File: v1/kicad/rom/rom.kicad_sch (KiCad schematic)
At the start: 2 parts, among them IC1 AT28C64B-15PU, U1 LNCPU Type A Connector

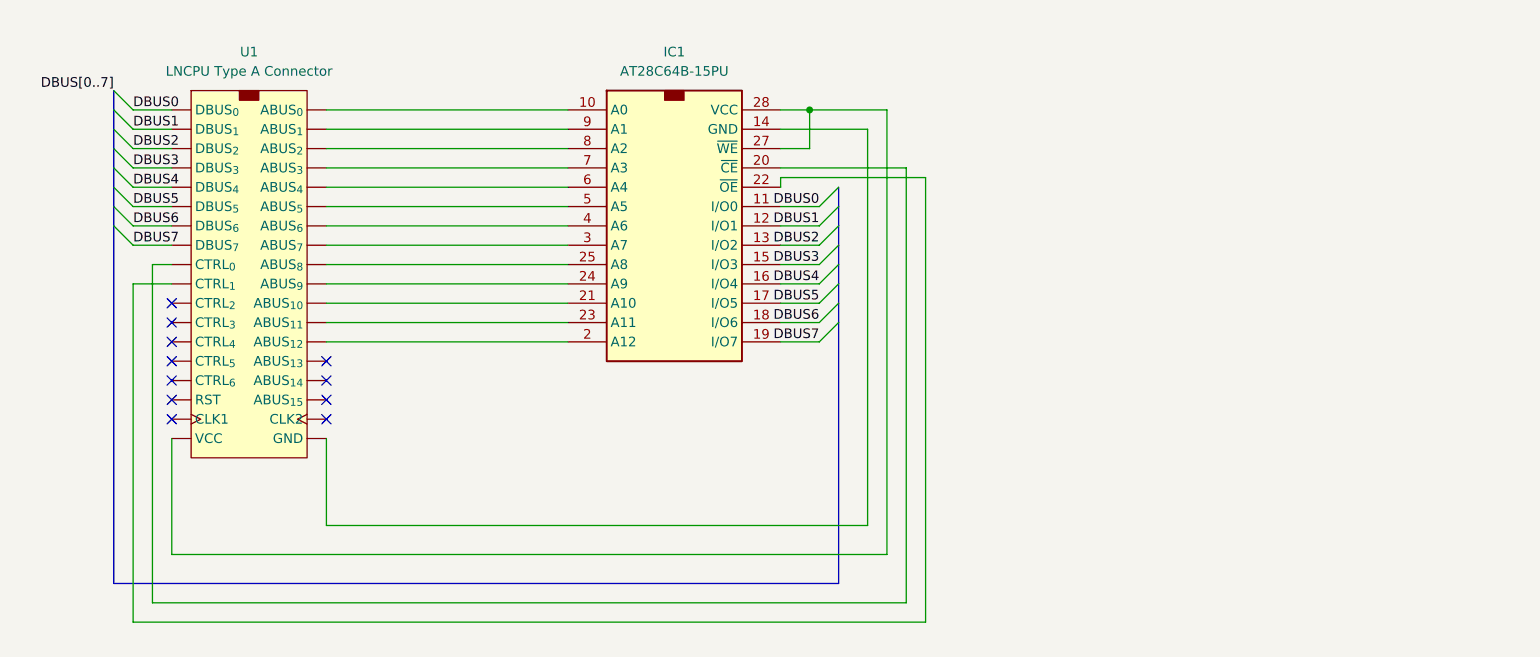
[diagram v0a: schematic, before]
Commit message: readapt designs for BR, SP, SR, ALU
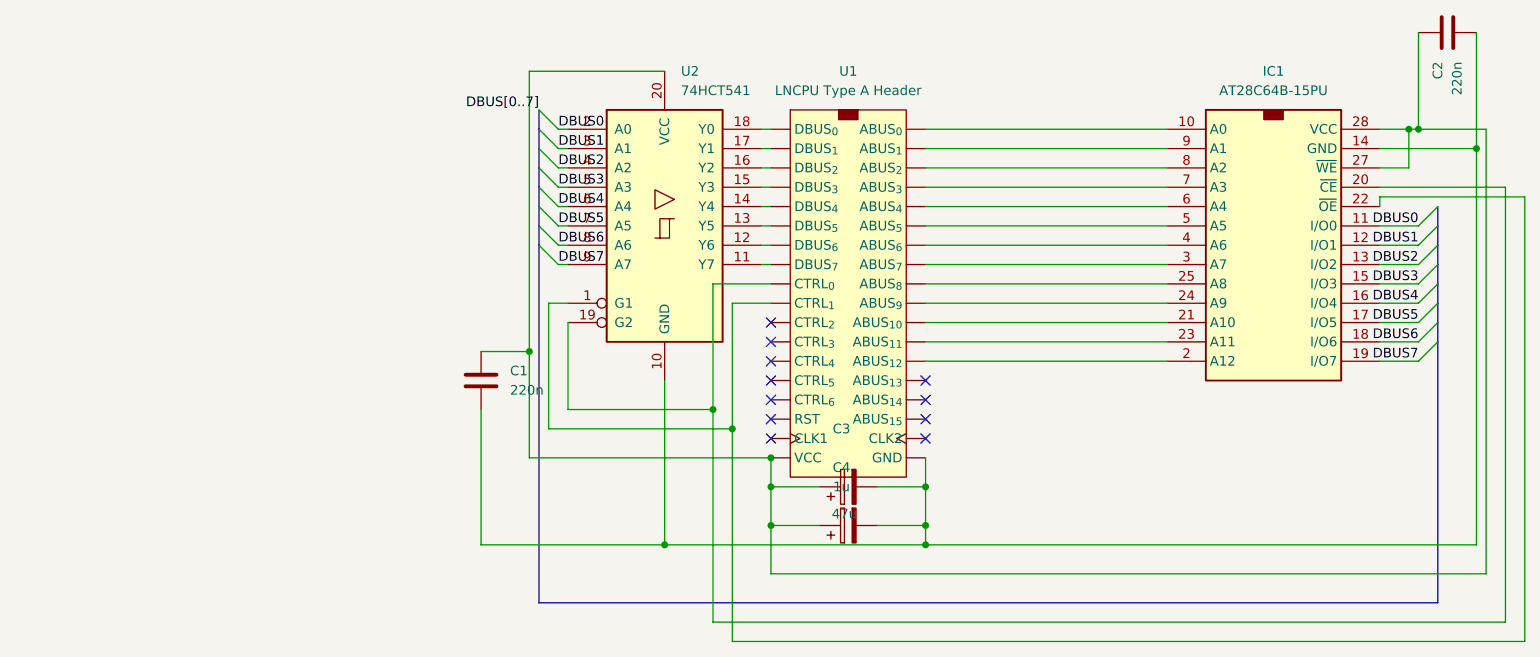
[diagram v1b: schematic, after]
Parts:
- added C1, C2: 220n, Capacitor_THT:C_Disc_D5.0mm_W2.5mm_P2.50mm, symbol Device:C
- added C3: 47u, Capacitor_THT:CP_Radial_D5.0mm_P2.00mm, symbol Device:C_Polarized
- added C4: 1u, lncpu:CP_Radial_D4.0mm_P2.00mm-Large-Holes, symbol Device:C_Polarized
- added U2: 74HCT541, Package_DIP:DIP-20_W7.62mm_LongPads, symbol 74xx:74HCT541
- U1: value LNCPU Type A Connector -> LNCPU Type A Header; symbol lncpu:LNCPU_Type_A_Connector -> lncpu:LNCPU_Type_A_Header
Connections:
- net DBUS0: now also U2.2 (A0); no longer U1.19 (DBUS_{0})
- net DBUS1: now also U2.3 (A1); no longer U1.21 (DBUS_{1})
- net DBUS2: now also U2.4 (A2); no longer U1.23 (DBUS_{2})
- net DBUS3: now also U2.5 (A3); no longer U1.25 (DBUS_{3})
- net DBUS4: now also U2.6 (A4); no longer U1.27 (DBUS_{4})
- net DBUS5: now also U2.7 (A5); no longer U1.29 (DBUS_{5})
- net DBUS6: now also U2.8 (A6); no longer U1.31 (DBUS_{6})
- net DBUS7: now also U2.9 (A7); no longer U1.33 (DBUS_{7})
- net at IC1.14 (GND), U1.1 (GND), U1.37 (GND)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: now also C1.2, C2.2, C3.2, C4.2, U2.10 (GND)
- net at IC1.27 (~{WE}), IC1.28 (VCC), U1.2 (VCC)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: now also C1.1, C2.1, C3.1, C4.1, U2.20 (VCC)
- net at IC1.20 (~{CE}), U1.3 (CTRL_{0}): now also U2.19 (G2)
- net at IC1.22 (~{OE}), U1.5 (CTRL_{1}): now also U2.1 (G1)
- new net: U1.19 (DBUS_{0}), U2.18 (Y0)
- new net: U1.21 (DBUS_{1}), U2.17 (Y1)
- new net: U1.23 (DBUS_{2}), U2.16 (Y2)
- new net: U1.25 (DBUS_{3}), U2.15 (Y3)
- new net: U1.27 (DBUS_{4}), U2.14 (Y4)
- new net: U1.29 (DBUS_{5}), U2.13 (Y5)
- new net: U1.31 (DBUS_{6}), U2.12 (Y6)
- new net: U1.33 (DBUS_{7}), U2.11 (Y7)
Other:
- moved on the sheet: IC1, U1
